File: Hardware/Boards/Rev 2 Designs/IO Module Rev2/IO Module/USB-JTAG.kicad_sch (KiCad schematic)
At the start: 42 parts, among them Q4 IRLML6244, U11 93LCxxBxxOT, U12 74AVC2T245GU, U8 74AVC4T774BQX, U9 FT2232HQ, Y1 12Mhz

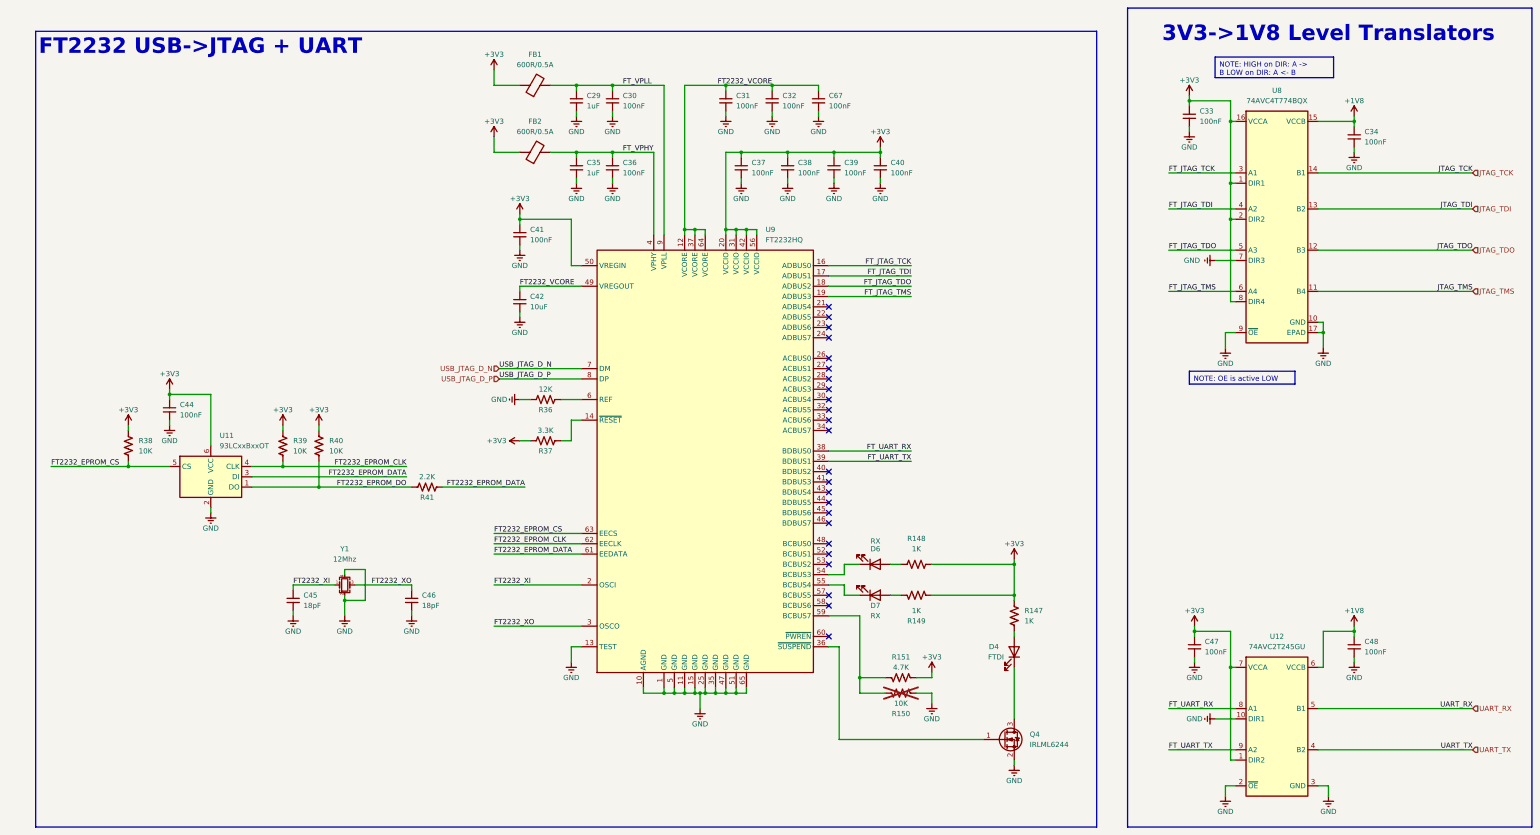
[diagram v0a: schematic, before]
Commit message: Rev 2 IO module complete
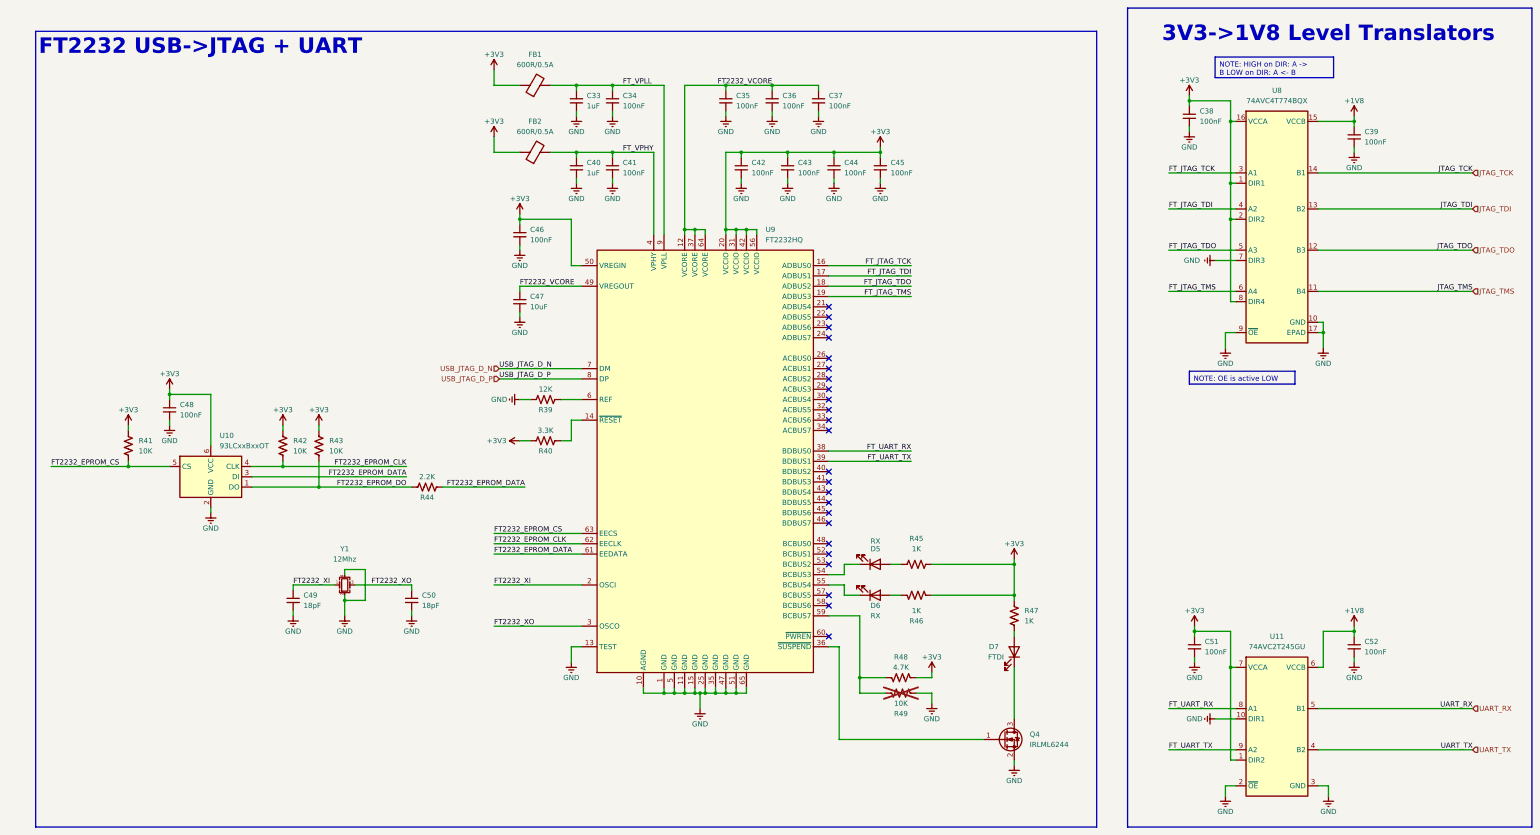
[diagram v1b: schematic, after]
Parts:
- renumbered C29 to C33, C30 to C34, C31 to C35, C32 to C36, C67 to C37, C33 to C38, C34 to C39, C35 to C40, C36 to C41, C37 to C42, C38 to C43, C39 to C44, C40 to C45, C41 to C46, C42 to C47, C44 to C48, C45 to C49, C46 to C50, C47 to C51, C48 to C52, D6 to D5, D7 to D6, D4 to D7, R36 to R39, R37 to R40, R38 to R41, R39 to R42, R40 to R43, R41 to R44, R148 to R45, R149 to R46, R147 to R47, R151 to R48, R150 to R49, U11 to U10, U12 to U11

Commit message: Updated Schematics & created pixel combiner HDL
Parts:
- R48: value 4.7K -> 10K
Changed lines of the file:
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@@
 			)
 		)
-		(property "Value" "4.7K"
+		(property "Value" "10K"
 			(at 234.95 199.39 90)
 			(effects
